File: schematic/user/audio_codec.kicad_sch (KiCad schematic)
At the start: 27 parts, among them U4 TLV320AIC3254IRHBR

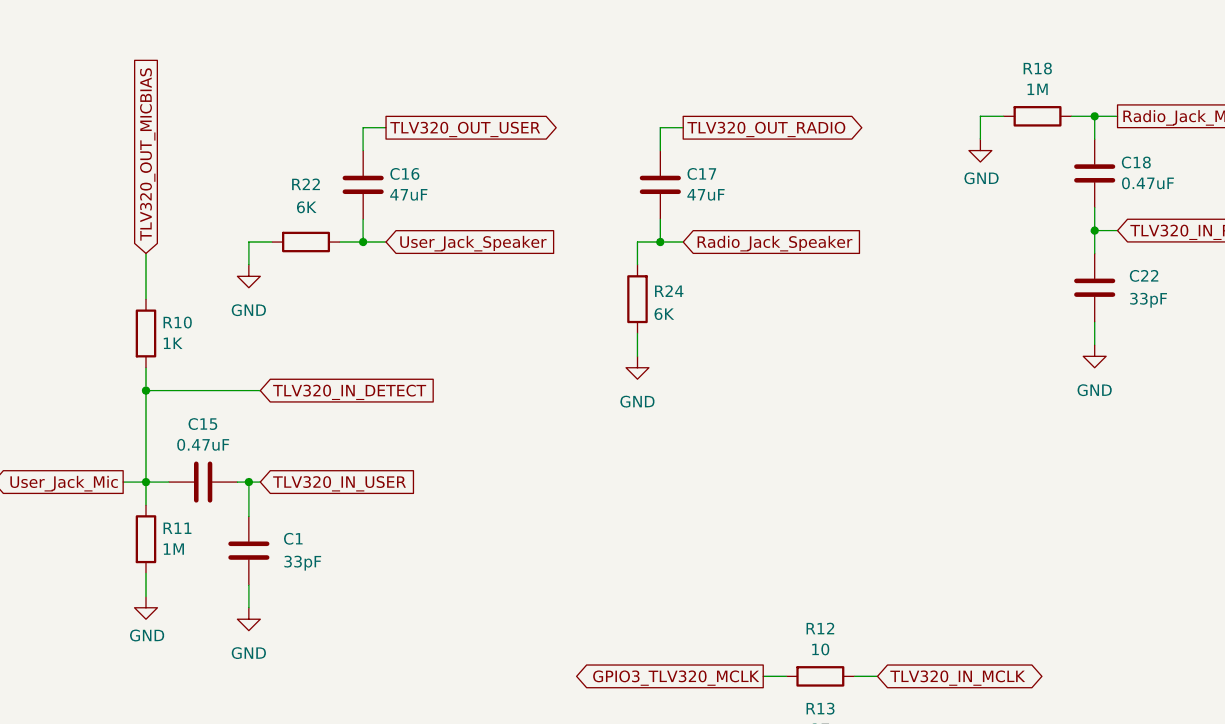
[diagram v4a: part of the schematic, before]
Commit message: v0.4 board: adjust pulldown resistors for audio I/O.
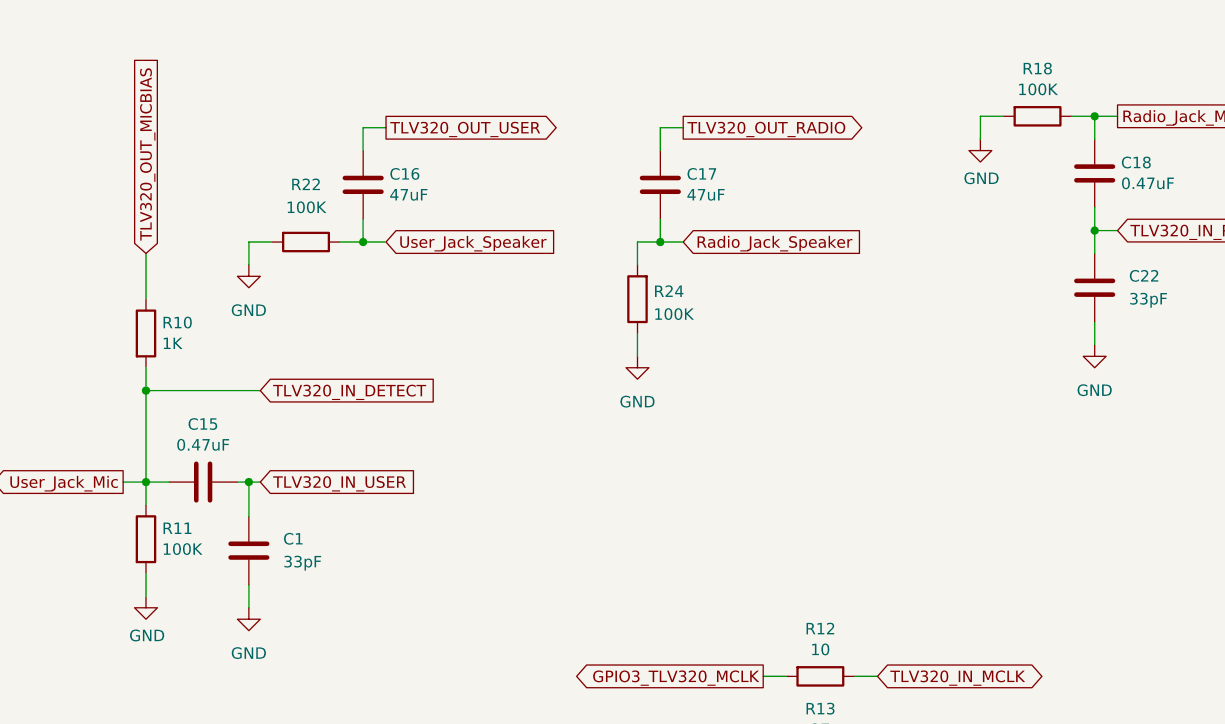
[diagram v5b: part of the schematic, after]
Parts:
- R11, R18: value 1M -> 100K; footprint Resistor_SMD:R_0603_1608Metric -> Resistor_SMD:R_0402_1005Metric; LCSC C22935 -> C25741
- R22, R24: value 6K -> 100K; LCSC C25908 -> C25741
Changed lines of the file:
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@@
     (in_bom yes) (on_board yes) (fields_autoplaced)
     (property "Reference" "R22" (id 0) (at 167.64 35.56 90))
-    (property "Value" "6K" (id 1) (at 167.64 38.1 90))
+    (property "Value" "100K" (id 1) (at 167.64 38.1 90))
     (property "Footprint" "Resistor_SMD:R_0402_1005Metric" (id 2) (at 167.64 40.132 90)
       (effects (font (size 1.27 1.27)) hide)
     )
-    (property "Datasheet" "https://datasheet.lcsc.com/lcsc/2206010045_UNI-ROYAL-Uniroyal-Elec-0402WGF5601TCE_C25908.pdf" (id 3) (at 167.64 41.91 0)
-      (effects (font (size 1.27 1.27)) hide)
-    )
-    (property "LCSC" "C25908" (id 4) (at 167.64 41.91 0)
+    (property "Datasheet" "https://datasheet.lcsc.com/lcsc/2206010100_UNI-ROYAL-Uniroyal-Elec-0402WGF1003TCE_C25741.pdf" (id 3) (at 167.64 41.91 0)
+      (effects (font (size 1.27 1.27)) hide)
+    )
+    (property "LCSC" "C25741" (id 4) (at 167.64 41.91 0)
       (effects (font (size 1.27 1.27)) hide)
     )
@@
       (effects (font (size 1.27 1.27)) (justify right))
     )
-    (property "Value" "6K" (id 1) (at 206.248 49.9622 0)
+    (property "Value" "100K" (id 1) (at 206.248 49.9622 0)
       (effects (font (size 1.27 1.27)) (justify right))
     )
@@
       (effects (font (size 1.27 1.27)) hide)
     )
-    (property "Datasheet" "https://datasheet.lcsc.com/lcsc/2206010045_UNI-ROYAL-Uniroyal-Elec-0402WGF5601TCE_C25908.pdf" (id 3) (at 204.47 48.26 0)
-      (effects (font (size 1.27 1.27)) hide)
-    )
-    (property "LCSC" "C25908" (id 4) (at 204.47 48.26 0)
+    (property "Datasheet" "https://datasheet.lcsc.com/lcsc/2206010100_UNI-ROYAL-Uniroyal-Elec-0402WGF1003TCE_C25741.pdf" (id 3) (at 204.47 48.26 0)
+      (effects (font (size 1.27 1.27)) hide)
+    )
+    (property "LCSC" "C25741" (id 4) (at 204.47 48.26 0)
       (effects (font (size 1.27 1.27)) hide)
     )
@@
     (in_bom yes) (on_board yes)
     (property "Reference" "R18" (id 0) (at 248.92 22.6822 90))
-    (property "Value" "1M" (id 1) (at 248.92 24.9936 90))
-    (property "Footprint" "Resistor_SMD:R_0603_1608Metric" (id 2) (at 248.92 26.162 90)
-      (effects (font (size 1.27 1.27)) hide)
-    )
-    (property "Datasheet" "https://datasheet.lcsc.com/lcsc/2110252030_UNI-ROYAL-Uniroyal-Elec-0603WAF1004T5E_C22935.pdf" (id 3) (at 248.92 27.94 0)
-      (effects (font (size 1.27 1.27)) hide)
-    )
-    (property "LCSC" "C22935" (id 4) (at 248.92 27.94 0)
+    (property "Value" "100K" (id 1) (at 248.92 24.9936 90))
+    (property "Footprint" "Resistor_SMD:R_0402_1005Metric" (id 2) (at 248.92 26.162 90)
+      (effects (font (size 1.27 1.27)) hide)
+    )
+    (property "Datasheet" "https://datasheet.lcsc.com/lcsc/2206010100_UNI-ROYAL-Uniroyal-Elec-0402WGF1003TCE_C25741.pdf" (id 3) (at 248.92 27.94 0)
+      (effects (font (size 1.27 1.27)) hide)
+    )
+    (property "LCSC" "C25741" (id 4) (at 248.92 27.94 0)
       (effects (font (size 1.27 1.27)) hide)
     )
@@
       (effects (font (size 1.27 1.27)) (justify left))
     )
-    (property "Value" "1M" (id 1) (at 151.638 76.073 0)
-      (effects (font (size 1.27 1.27)) (justify left))
-    )
-    (property "Footprint" "Resistor_SMD:R_0603_1608Metric" (id 2) (at 148.082 74.93 90)
-      (effects (font (size 1.27 1.27)) hide)
-    )
-    (property "Datasheet" "https://datasheet.lcsc.com/lcsc/2110252030_UNI-ROYAL-Uniroyal-Elec-0603WAF1004T5E_C22935.pdf" (id 3) (at 149.86 74.93 0)
-      (effects (font (size 1.27 1.27)) hide)
-    )
-    (property "LCSC" "C22935" (id 4) (at 149.86 74.93 0)
-      (effects (font (size 1.27 1.27)) hide)
-    )
+    (property "Value" "100K" (id 1) (at 151.638 76.073 0)
+      (effects (font (size 1.27 1.27)) (justify left))
+    )
+    (property "Footprint" "Resistor_SMD:R_0402_1005Metric" (id 2) (at 148.082 74.93 90)
+      (effects (font (size 1.27 1.27)) hide)
+    )
+    (property "Datasheet" "https://datasheet.lcsc.com/lcsc/2206010100_UNI-ROYAL-Uniroyal-Elec-0402WGF1003TCE_C25741.pdf" (id 3) (at 149.86 74.93 0)
+      (effects (font (size 1.27 1.27)) hide)
+    )
+    (property "LCSC" "C25741" (id 4) (at 149.86 74.93 0)
+      (effects (font (size 1.27 1.27)) hide)
+    )

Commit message: v0.4 board submitted for build/assembly.
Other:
- company: (none) -> FreeDV Project
- title: (none) -> ezDV Audio Codec
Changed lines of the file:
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@@
 (kicad_sch (version 20211123) (generator eeschema)
   (paper "A4")
+  (title_block
+    (title "ezDV Audio Codec")
+    (date "2022-10-01")
+    (rev "v0.4")
+    (company "FreeDV Project")
+  )
   (junction (at 49.53 88.9) (diameter 0) (color 0 0 0 0)
   )

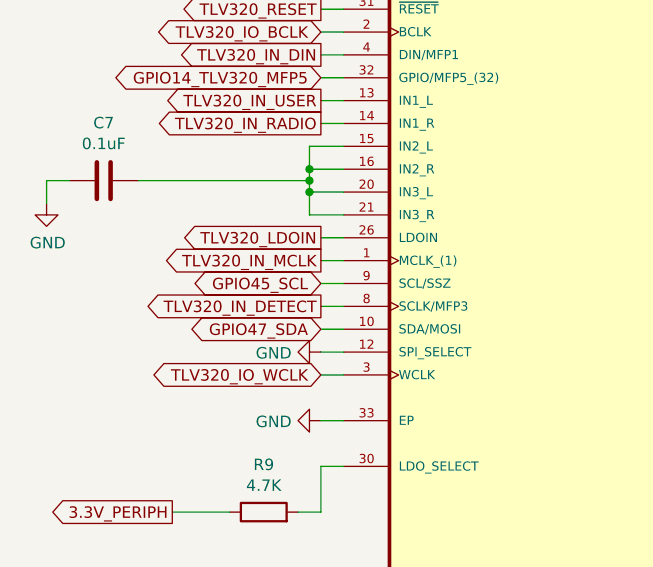
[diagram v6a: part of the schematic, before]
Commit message: v0.5 board: move SCL to GPIO 48 as 45 is a ESP32 strapping pin.
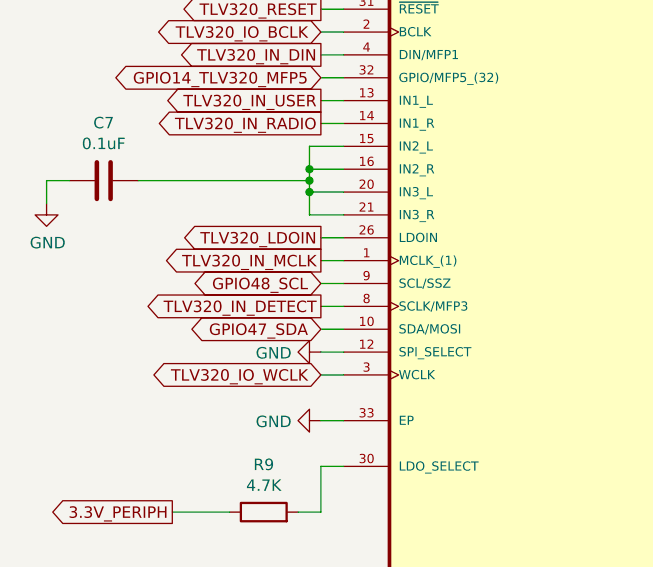
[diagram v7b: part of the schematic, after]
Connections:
- net GPIO45_SCL renamed GPIO48_SCL
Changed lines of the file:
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@@
     )
   )
-  (global_label "GPIO45_SCL" (shape bidirectional) (at 50.8 99.06 180) (fields_autoplaced)
+  (global_label "GPIO48_SCL" (shape bidirectional) (at 50.8 99.06 180) (fields_autoplaced)
     (effects (font (size 1.27 1.27)) (justify right))
     (property "Intersheet References" "${INTERSHEET_REFS}" (id 0) (at 37.0174 98.9806 0)
